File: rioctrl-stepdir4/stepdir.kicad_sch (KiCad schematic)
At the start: 19 parts, among them J3 RJ45_LED_Shielded, Q5 BSS138W, Q6 AO3401A, U1 CS48505S, U2 CS48505S, U6 USBLC6-4SC6

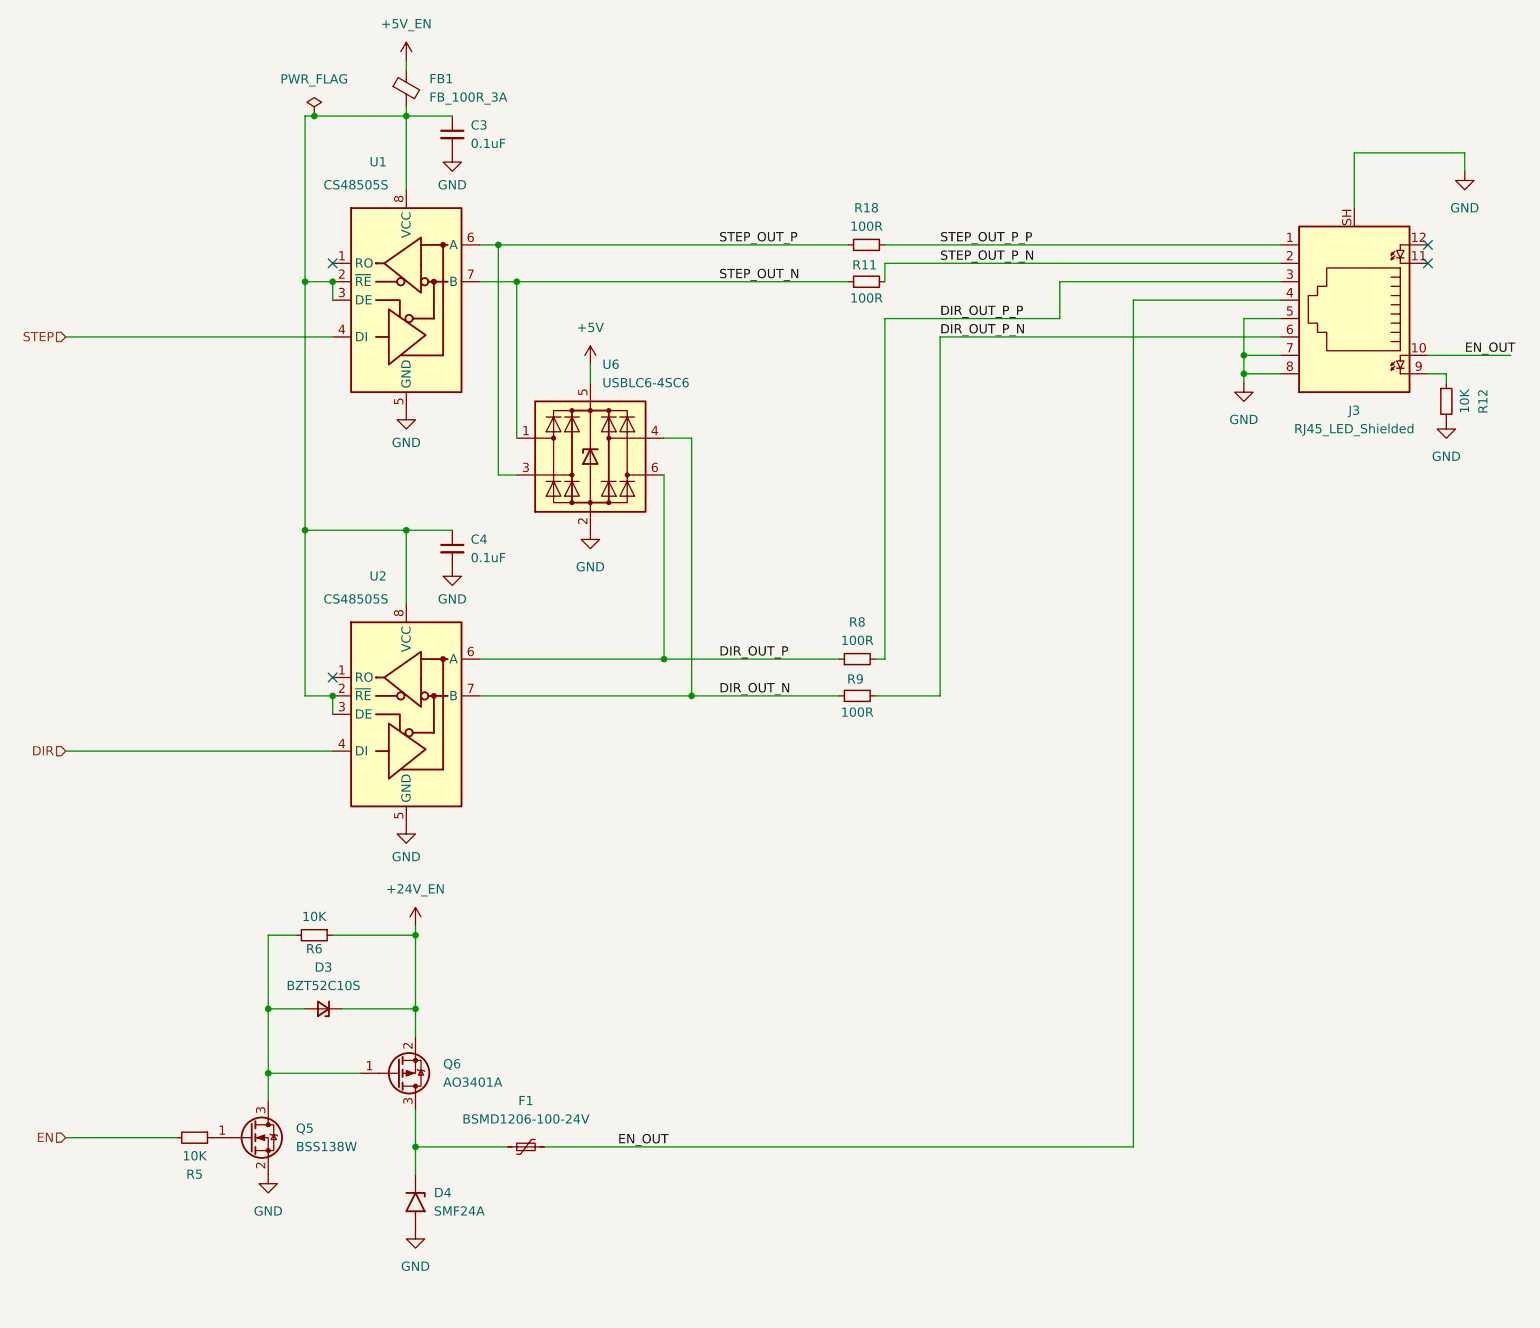
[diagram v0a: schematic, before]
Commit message: Label axes on stepdir
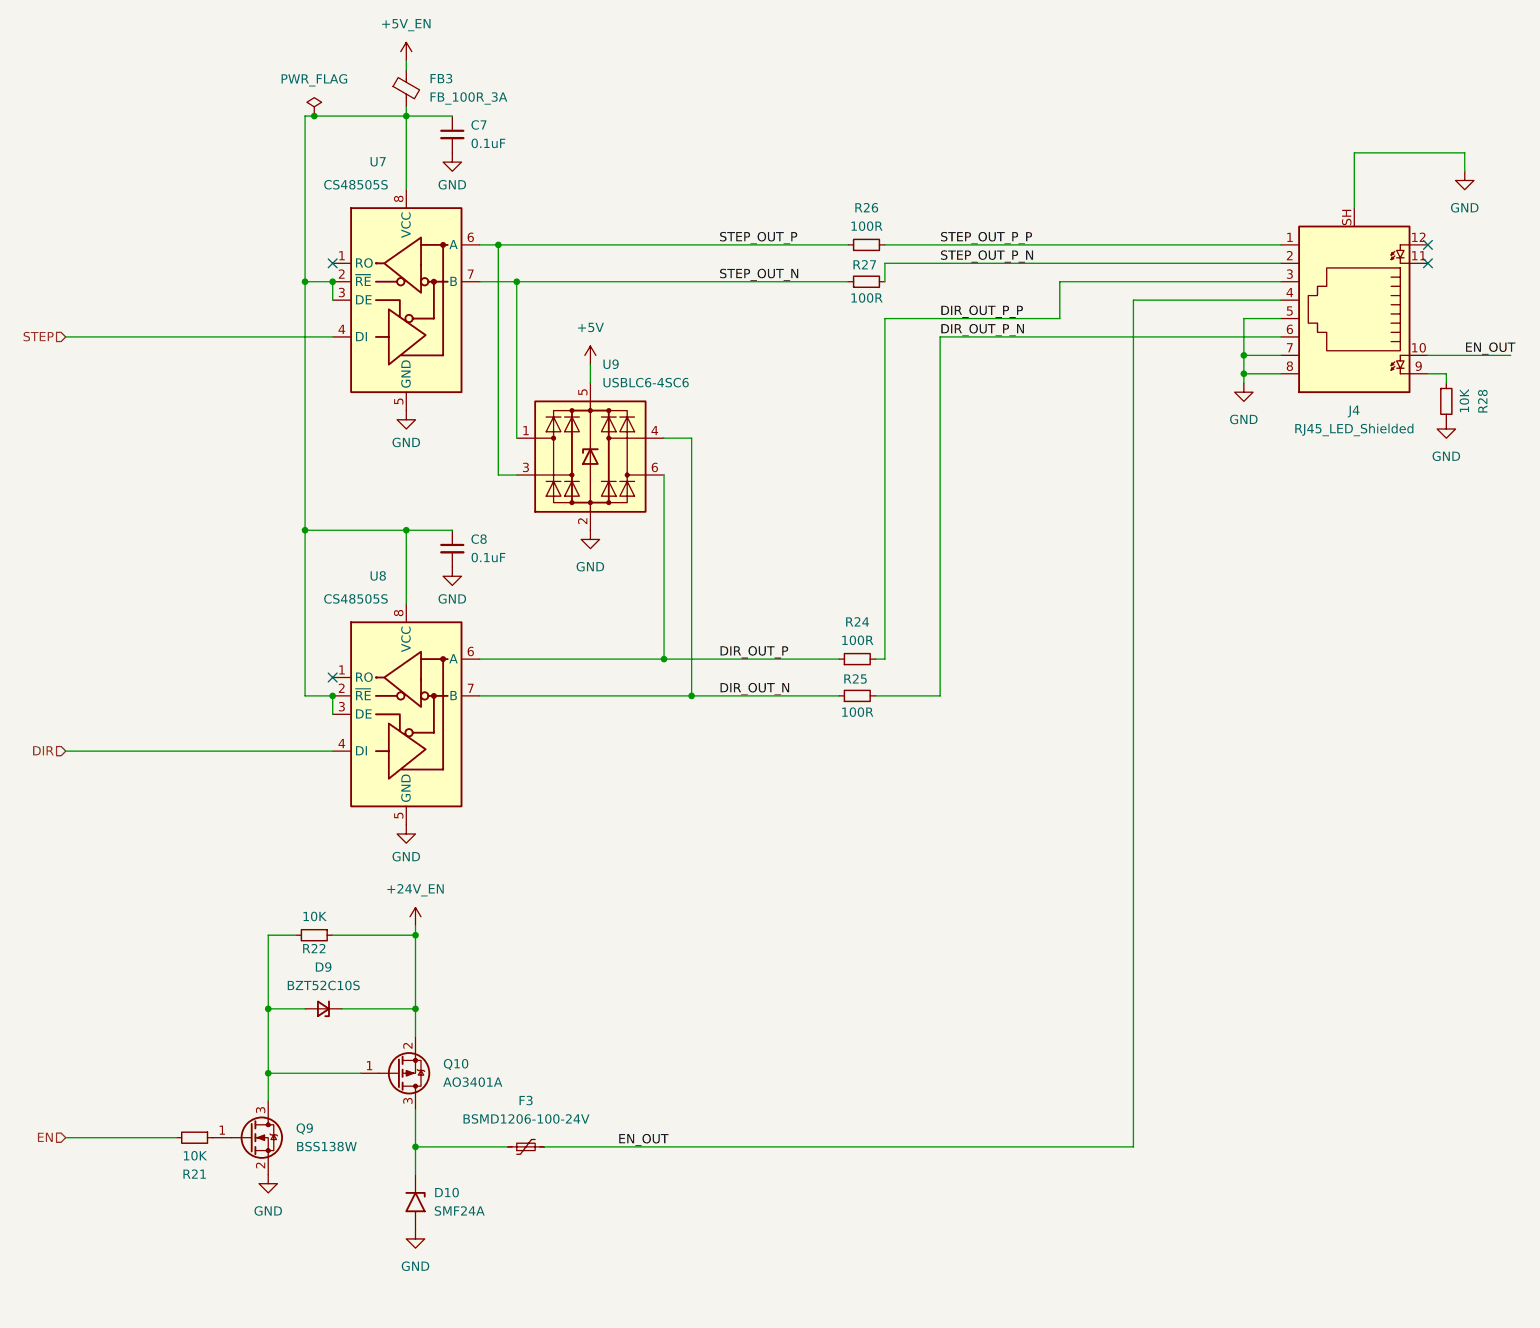
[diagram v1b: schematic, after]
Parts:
- renumbered C3 to C7, C4 to C8, D4 to D10, D3 to D9, F1 to F3, FB1 to FB3, J3 to J4, Q6 to Q10, Q5 to Q9, R5 to R21, R6 to R22, R8 to R24, R9 to R25, R18 to R26, R11 to R27, R12 to R28, U1 to U7, U2 to U8, U6 to U9
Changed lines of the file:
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@@
 		(on_board yes)
 		(dnp no)
-		(property "Reference" "R6"
+		(property "Reference" "R22"
 			(at 86.36 141.605 90)
 			(effects
@@
 		(dnp no)
 		(fields_autoplaced yes)
-		(property "Reference" "R8"
+		(property "Reference" "R24"
 			(at 161.29 96.52 90)
 			(effects
@@
 		(dnp no)
 		(fields_autoplaced yes)
-		(property "Reference" "#PWR018"
+		(property "Reference" "#PWR046"
 			(at 99.06 130.81 0)
 			(effects
@@
 		(dnp no)
 		(fields_autoplaced yes)
-		(property "Reference" "Q6"
+		(property "Reference" "Q10"
 			(at 104.14 157.48 0)
 			(effects
@@
 		(dnp no)
 		(fields_autoplaced yes)
-		(property "Reference" "D3"
+		(property "Reference" "D9"
 			(at 87.63 144.145 0)
 			(effects
@@
 		(dnp no)
 		(fields_autoplaced yes)
-		(property "Reference" "C3"
+		(property "Reference" "C7"
 			(at 107.95 27.9463 0)
 			(effects
@@
 		(dnp no)
 		(fields_autoplaced yes)
-		(property "Reference" "#PWR030"
+		(property "Reference" "#PWR044"
 			(at 99.06 22.86 0)
 			(effects
@@
 		(on_board yes)
 		(dnp no)
-		(property "Reference" "U1"
+		(property "Reference" "U7"
 			(at 93.98 33.02 0)
 			(effects
@@
 		(dnp no)
 		(fields_autoplaced yes)
-		(property "Reference" "#FLG07"
+		(property "Reference" "#FLG09"
 			(at 86.36 24.765 0)
 			(effects
@@
 		(dnp no)
 		(fields_autoplaced yes)
-		(property "Reference" "#PWR022"
+		(property "Reference" "#PWR050"
 			(at 105.41 95.25 0)
 			(effects
@@
 		(dnp no)
 		(fields_autoplaced yes)
-		(property "Reference" "U6"
+		(property "Reference" "U9"
 			(at 126.1111 60.96 0)
 			(effects
@@
 		(on_board yes)
 		(dnp no)
-		(property "Reference" "R12"
+		(property "Reference" "R28"
 			(at 247.65 66.04 90)
 			(effects
@@
 		(dnp no)
 		(fields_autoplaced yes)
-		(property "Reference" "#PWR017"
+		(property "Reference" "#PWR045"
 			(at 99.06 73.66 0)
 			(effects
@@
 		(dnp no)
 		(fields_autoplaced yes)
-		(property "Reference" "J3"
+		(property "Reference" "J4"
 			(at 229.87 67.31 0)
 			(effects
@@
 		(dnp no)
 		(fields_autoplaced yes)
-		(property "Reference" "F1"
+		(property "Reference" "F3"
 			(at 115.57 162.56 90)
 			(effects
@@
 		(dnp no)
 		(fields_autoplaced yes)
-		(property "Reference" "FB1"
+		(property "Reference" "FB3"
 			(at 102.235 21.5519 0)
 			(effects
@@
 		(dnp no)
 		(fields_autoplaced yes)
-		(property "Reference" "#PWR027"
+		(property "Reference" "#PWR055"
 			(at 242.57 74.93 0)
 			(effects
@@
 		(on_board yes)
 		(dnp no)
-		(property "Reference" "U2"
+		(property "Reference" "U8"
 			(at 93.98 90.17 0)
 			(effects
@@
 		(dnp no)
 		(fields_autoplaced yes)
-		(property "Reference" "C4"
+		(property "Reference" "C8"
 			(at 107.95 85.0963 0)
 			(effects
@@
 		(on_board yes)
 		(dnp no)
-		(property "Reference" "R9"
+		(property "Reference" "R25"
 			(at 161.036 104.394 90)
 			(effects
@@
 		(dnp no)
 		(fields_autoplaced yes)
-		(property "Reference" "#PWR019"
+		(property "Reference" "#PWR033"
 			(at 100.33 142.24 0)
 			(effects
@@
 		(dnp no)
 		(fields_autoplaced yes)
-		(property "Reference" "#PWR021"
+		(property "Reference" "#PWR049"
 			(at 105.41 38.1 0)
 			(effects
@@
 		(on_board yes)
 		(dnp no)
-		(property "Reference" "R11"
+		(property "Reference" "R27"
 			(at 162.306 47.244 90)
 			(effects
@@
 		(dnp no)
 		(fields_autoplaced yes)
-		(property "Reference" "D4"
+		(property "Reference" "D10"
 			(at 102.87 175.26 90)
 			(effects
@@
 		(on_board yes)
 		(dnp no)
-		(property "Reference" "R5"
+		(property "Reference" "R21"
 			(at 69.85 172.72 90)
 			(effects
@@
 		(dnp no)
 		(fields_autoplaced yes)
-		(property "Reference" "#PWR020"
+		(property "Reference" "#PWR048"
 			(at 100.33 186.69 0)
 			(effects
@@
 		(dnp no)
 		(fields_autoplaced yes)
-		(property "Reference" "R18"
+		(property "Reference" "R26"
 			(at 162.56 39.37 90)
 			(effects
@@
 		(dnp no)
 		(fields_autoplaced yes)
-		(property "Reference" "#PWR038"
+		(property "Reference" "#PWR052"
 			(at 124.46 64.77 0)
 			(effects
@@
 		(dnp no)
 		(fields_autoplaced yes)
-		(property "Reference" "#PWR015"
+		(property "Reference" "#PWR043"
 			(at 80.01 179.07 0)
 			(effects
@@
 		(dnp no)
 		(fields_autoplaced yes)
-		(property "Reference" "#PWR040"
+		(property "Reference" "#PWR054"
 			(at 214.63 69.85 0)
 			(effects
@@
 		(dnp no)
 		(fields_autoplaced yes)
-		(property "Reference" "#PWR042"
+		(property "Reference" "#PWR056"
 			(at 245.11 40.64 0)
 			(effects
@@
 		(dnp no)
 		(fields_autoplaced yes)
-		(property "Reference" "Q5"
+		(property "Reference" "Q9"
 			(at 83.82 166.37 0)
 			(effects
@@
 		(dnp no)
 		(fields_autoplaced yes)
-		(property "Reference" "#PWR025"
+		(property "Reference" "#PWR053"
 			(at 124.46 90.17 0)
 			(effects

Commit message: Fix ERC, add title information to sch, add initial version of build scripts
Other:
- company: (none) -> R. Veips
- title: (none) -> rioctrl-stepdir4
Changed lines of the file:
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@@
 	(generator_version "8.0")
 	(paper "A4")
+	(title_block
+		(title "rioctrl-stepdir4")
+		(date "2024-08-25")
+		(rev "${VERSION}")
+		(company "R. Veips")
+	)
 	(junction
 		(at 99.06 26.67)

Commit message: Fill in BOM (LCSC#)
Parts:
- C7, C8: LCSC# (none) -> C14663
- R21, R22, R28: LCSC# (none) -> C98220
- R24, R25, R26, R27: LCSC# (none) -> C105588
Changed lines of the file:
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@@
+			)
+		)
+		(property "LCSC#" "C98220"
+			(at 86.36 139.7 0)
+			(effects
+				(font
+					(size 1.27 1.27)
+				)
+				(hide yes)
 			)
 		)
@@
 			)
 		)
+		(property "LCSC#" "C105588"
+			(at 161.29 101.6 0)
+			(effects
+				(font
+					(size 1.27 1.27)
+				)
+				(hide yes)
+			)
+		)
 		(pin "2"
 		)
@@
 			)
 		)
+		(property "LCSC#" "C14663"
+			(at 105.41 29.21 0)
+			(effects
+				(font
+					(size 1.27 1.27)
+				)
+				(hide yes)
+			)
+		)
 		(pin "1"
 		)
@@
 			)
 		)
+		(property "LCSC#" "C98220"
+			(at 242.57 66.04 0)
+			(effects
+				(font
+					(size 1.27 1.27)
+				)
+				(hide yes)
+			)
+		)
 		(pin "1"
 		)
@@
 			)
 		)
+		(property "LCSC#" "C14663"
+			(at 105.41 86.36 0)
+			(effects
+				(font
+					(size 1.27 1.27)
+				)
+				(hide yes)
+			)
+		)
 		(pin "1"
 		)
@@
 		)
 		(property "Description" "Resistor, small symbol"
+			(at 161.29 106.68 0)
+			(effects
+				(font
+					(size 1.27 1.27)
+				)
+				(hide yes)
+			)
+		)
+		(property "LCSC#" "C105588"
 			(at 161.29 106.68 0)
 			(effects
@@
 			)
 		)
+		(property "LCSC#" "C105588"
+			(at 162.56 49.53 0)
+			(effects
+				(font
+					(size 1.27 1.27)
+				)
+				(hide yes)
+			)
+		)
 		(pin "2"
 		)
@@
 			)
 		)
+		(property "LCSC#" "C98220"
+			(at 69.85 167.64 0)
+			(effects
+				(font
+					(size 1.27 1.27)
+				)
+				(hide yes)
+			)
+		)
 		(pin "1"
 		)
@@
 			(at 162.56 44.45 0)
 			(effects
+				(font
+					(size 1.27 1.27)
+				)
+				(hide yes)
+			)
+		)
+		(property "LCSC#" "C105588"
+			(at 162.56 44.45 0)
+			(effects

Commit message: Add forgotten series resistor for 24V output transistors in rioctrl-stepdir4
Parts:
- added R15: 10K, Resistor_SMD:R_0603_1608Metric, symbol Device:R_Small
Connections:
- net at D9.2 (A), Q10.1 (G), R22.2: now also R15.1; no longer Q9.3 (D)
- new net: Q9.3 (D), R15.2
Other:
- moved on the sheet: Q9, R21
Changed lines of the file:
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@@
 	(wire
 		(pts
-			(xy 52.07 167.64) (xy 67.31 167.64)
+			(xy 52.07 180.34) (xy 67.31 180.34)
 		)
 		(stroke
@@
 	(wire
 		(pts
-			(xy 80.01 158.75) (xy 80.01 162.56)
+			(xy 80.01 158.75) (xy 80.01 165.1)
 		)
 		(stroke
@@
 	(wire
 		(pts
+			(xy 80.01 170.18) (xy 80.01 175.26)
+		)
+		(stroke
+			(width 0)
+			(type default)
+		)
+	)
+	(wire
+		(pts
 			(xy 99.06 83.82) (xy 99.06 93.98)
 		)
@@
 	(hierarchical_label "EN"
 		(shape input)
-		(at 52.07 167.64 180)
+		(at 52.07 180.34 180)
 		(fields_autoplaced yes)
 		(effects
@@
 	(symbol
 		(lib_id "Device:R_Small")
-		(at 69.85 167.64 270)
+		(at 69.85 180.34 270)
 		(unit 1)
 		(exclude_from_sim no)
@@
 		(dnp no)
 		(property "Reference" "R21"
-			(at 69.85 172.72 90)
+			(at 69.85 185.42 90)
 			(effects
 				(font
@@
 		)
 		(property "Value" "10K"
-			(at 69.85 170.18 90)
+			(at 69.85 182.88 90)
 			(effects
 				(font
@@
 		)
 		(property "Footprint" "Resistor_SMD:R_0603_1608Metric"
-			(at 69.85 167.64 0)
+			(at 69.85 180.34 0)
 			(effects
 				(font
@@
 		)
 		(property "Datasheet" "~"
-			(at 69.85 167.64 0)
+			(at 69.85 180.34 0)
 			(effects
 				(font
@@
 		)
 		(property "Description" ""
-			(at 69.85 167.64 0)
+			(at 69.85 180.34 0)
 			(effects
 				(font
@@
 		)
 		(property "LCSC#" "C98220"
-			(at 69.85 167.64 0)
+			(at 69.85 180.34 0)
 			(effects
 				(font
@@
 	)
 	(symbol
+		(lib_id "Device:R_Small")
+		(at 80.01 167.64 0)
+		(unit 1)
+		(exclude_from_sim no)
+		(in_bom yes)
+		(on_board yes)
+		(dnp no)
+		(property "Reference" "R15"
+			(at 83.058 169.164 0)
+			(effects
+				(font
+					(size 1.27 1.27)
+				)
+			)
+		)
+		(property "Value" "10K"
+			(at 76.2 168.656 0)
+			(effects
+				(font
+					(size 1.27 1.27)
+				)
+			)
+		)
+		(property "Footprint" "Resistor_SMD:R_0603_1608Metric"
+			(at 80.01 167.64 0)
+			(effects
+				(font
+					(size 1.27 1.27)
+				)
+				(hide yes)
+			)
+		)
+		(property "Datasheet" "~"
+			(at 80.01 167.64 0)
+			(effects
+				(font
+					(size 1.27 1.27)
+				)
+				(hide yes)
+			)
+		)
+		(property "Description" ""
+			(at 80.01 167.64 0)
+			(effects
+				(font
+					(size 1.27 1.27)
+				)
+				(hide yes)
+			)
+		)
+		(property "LCSC#" "C98220"
+			(at 80.01 167.64 0)
+			(effects
+				(font
+					(size 1.27 1.27)
+				)
+				(hide yes)
+			)
+		)
+		(pin "1"
+		)
+		(pin "2"
+		)
+		(instances
+			(project "rioctrl-stepdir4"
+				(path "/09587842-9628-4761-8ca3-5c7cdb77bd67/05836d8b-9c0a-4ec5-b5c3-59f72c542683"
+					(reference "R31")
+					(unit 1)
+				)
+				(path "/09587842-9628-4761-8ca3-5c7cdb77bd67/37660470-539d-4ef0-8319-4a3363bab027"
+					(reference "R37")
+					(unit 1)
+				)
+				(path "/09587842-9628-4761-8ca3-5c7cdb77bd67/6edbf5bb-a097-4513-bbfc-fc51b4716a77"
+					(reference "R23")
+					(unit 1)
+				)
+				(path "/09587842-9628-4761-8ca3-5c7cdb77bd67/eebf3392-0a38-4e82-919d-cd3d193b6f43"
+					(reference "R15")
+					(unit 1)
+				)
+			)
+		)
+	)
+	(symbol
 		(lib_id "power:GND")
-		(at 80.01 172.72 0)
+		(at 80.01 185.42 0)
 		(unit 1)
 		(exclude_from_sim no)
@@
 		(fields_autoplaced yes)
 		(property "Reference" "#PWR043"
-			(at 80.01 179.07 0)
+			(at 80.01 191.77 0)
 			(effects
 				(font
@@
 		)
 		(property "Value" "GND"
-			(at 80.01 177.8 0)
+			(at 80.01 190.5 0)
 			(effects
 				(font
@@
 		)
 		(property "Footprint" ""
-			(at 80.01 172.72 0)
+			(at 80.01 185.42 0)
 			(effects
 				(font
@@
 		)
 		(property "Datasheet" ""
-			(at 80.01 172.72 0)
+			(at 80.01 185.42 0)
 			(effects
 				(font
@@
 		)
 		(property "Description" "Power symbol creates a global label with name \"GND\" , ground"
-			(at 80.01 172.72 0)
+			(at 80.01 185.42 0)
 			(effects
 				(font
@@
 	(symbol
 		(lib_id "hadv-transistors:BSS138W")
-		(at 77.47 167.64 0)
+		(at 77.47 180.34 0)
 		(unit 1)
 		(exclude_from_sim no)
@@
 		(fields_autoplaced yes)
 		(property "Reference" "Q9"
-			(at 83.82 166.37 0)
+			(at 83.82 179.07 0)
 			(effects
 				(font
@@
 		)
 		(property "Value" "BSS138W"
-			(at 83.82 168.91 0)
+			(at 83.82 181.61 0)
 			(effects
 				(font
@@
 		)
 		(property "Footprint" "Package_TO_SOT_SMD:SOT-323_SC-70"
-			(at 82.55 165.1 0)
+			(at 82.55 177.8 0)
 			(effects
 				(font
@@
 		)
 		(property "Datasheet" "~"
-			(at 77.47 167.64 0)
+			(at 77.47 180.34 0)
 			(effects
 				(font
@@
 		)
 		(property "Description" ""
-			(at 77.47 167.64 0)
+			(at 77.47 180.34 0)
 			(effects
 				(font
@@
 		)
 		(property "MPN" "BSS138W"
-			(at 77.47 167.64 0)
+			(at 77.47 180.34 0)
 			(effects
 				(font
@@
 		)
 		(property "Manufacturer" "Jiangsu Changjing Electronics Technology Co., Ltd."
-			(at 77.47 167.64 0)
+			(at 77.47 180.34 0)
 			(effects
 				(font
@@
 		)
 		(property "LCSC#" "C504052"
-			(at 77.47 167.64 0)
+			(at 77.47 180.34 0)
 			(effects
 				(font
